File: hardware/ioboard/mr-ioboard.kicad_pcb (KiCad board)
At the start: 4 copper layers, 65 x 80 mm, 126 parts, among them J1 Conn_01x40_Shielded, J2 USB_C_Receptacle_USB2.0, J3 Conn_01x06, J4 Micro_SD_Card_Det, J5 Conn_01x04, J6 Conn_01x02, Q1 2N7002, SW1 SW_Push, U1 TPS62822, U10 F1C200S, U11 TPS54202DDC, U2 TPS56637, U3 TPD2E2U06, U4 DS90C363, U5 TPD2E2U06, U6 LD3985M28R_SOT23, U7 TPS62822, U8 FUSB302BMPX, U9 TPD2E2U06, Y1 24MHz

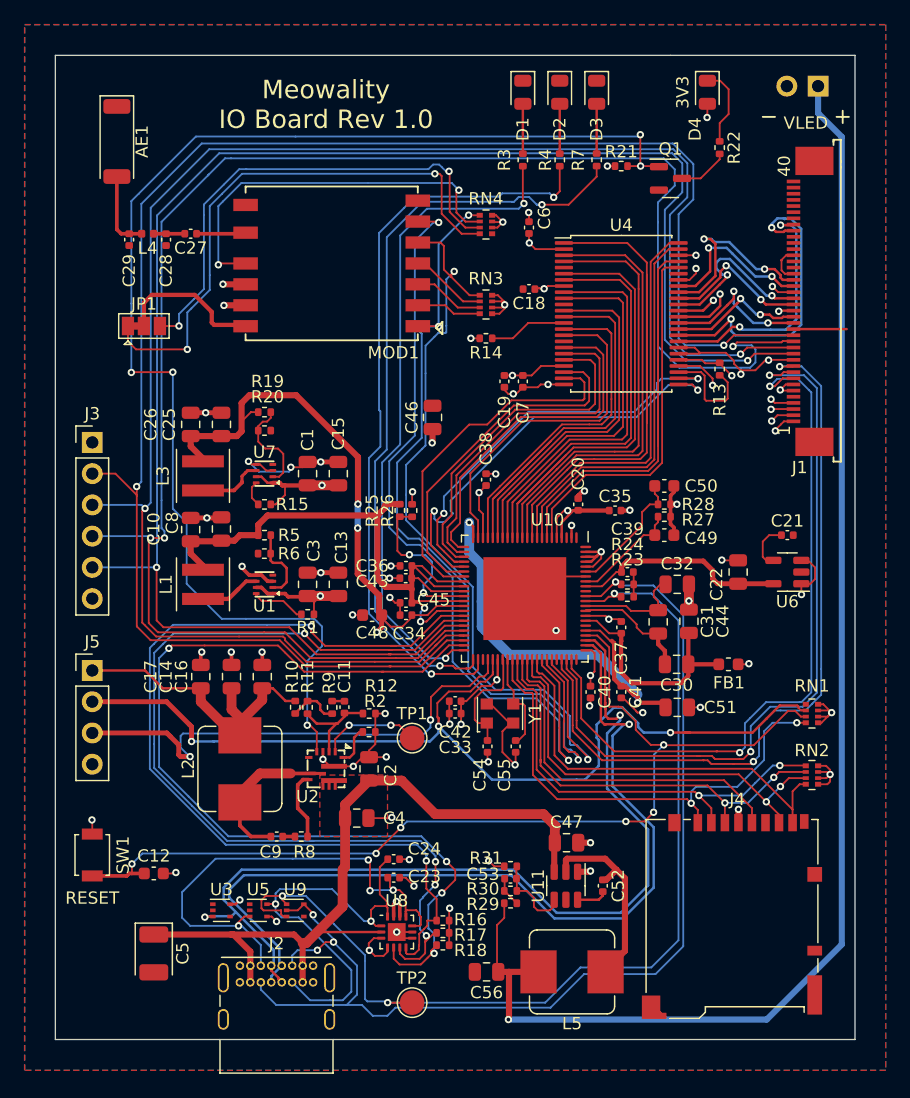
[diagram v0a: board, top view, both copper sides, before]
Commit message: Some tidying up of IO board
Signed-off-by: gatecat <gatecat@ds0.me>
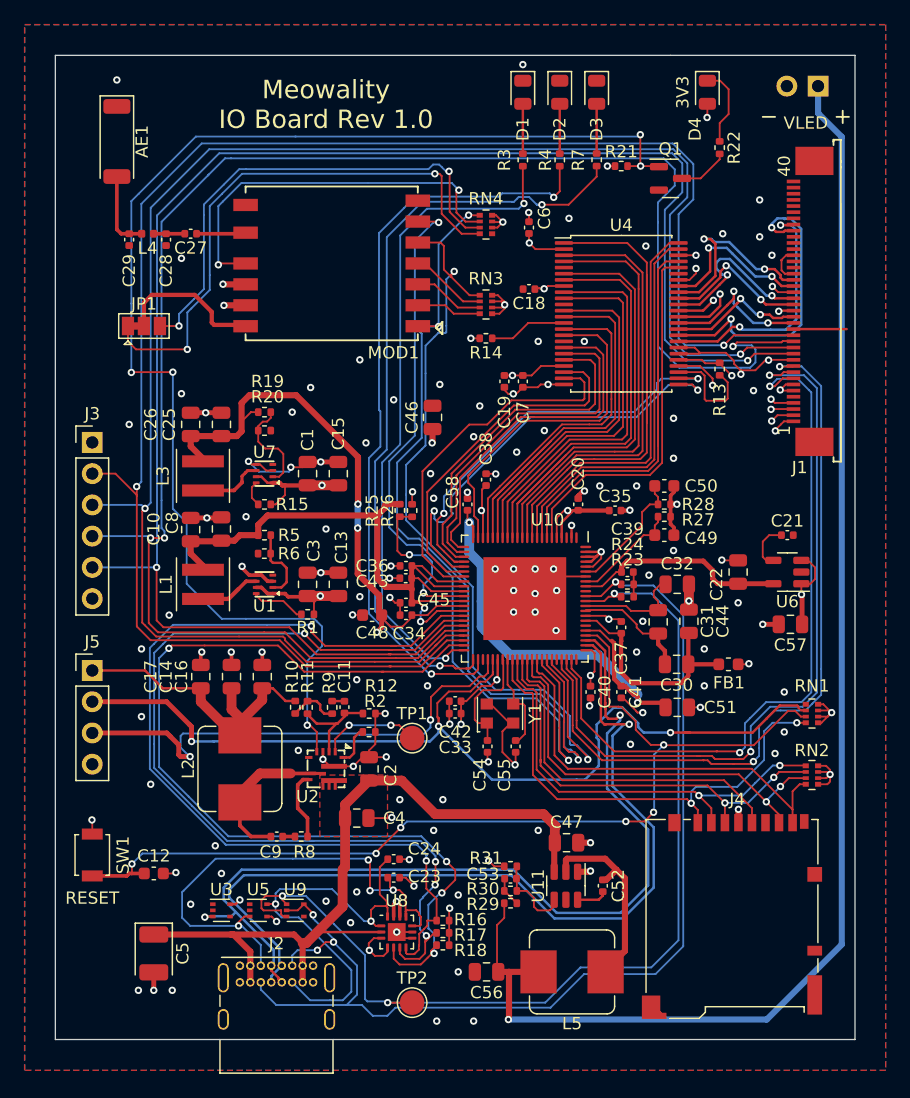
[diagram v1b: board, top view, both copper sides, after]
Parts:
- added C57: 10µ, Capacitor_SMD:C_0805_2012Metric, F.Cu at (159.8, 96.2)
- added C58: 470n, Capacitor_SMD:C_0402_1005Metric, F.Cu at (133.5, 86.5)
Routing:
- net GND: track 138.4 -> 141.6 mm, vias 57 -> 136
- net +3V3: track 138.3 -> 140.7 mm
- net +1V1: track 96.6 -> 97.7 mm

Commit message: Fix side of connector on IO board
Signed-off-by: gatecat <gatecat@ds0.me>
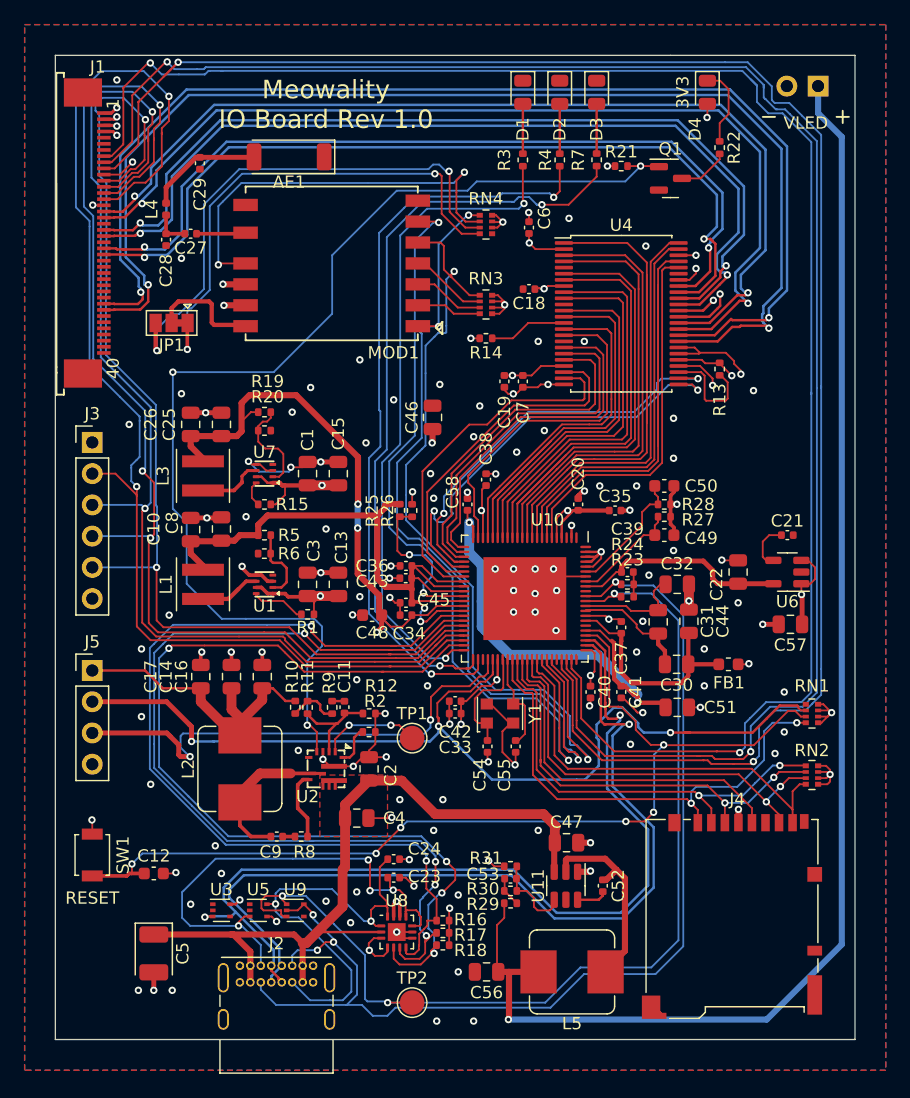
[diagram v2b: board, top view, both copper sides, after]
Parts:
- moved J1 56.3 mm to (103.9, 64.4), turned to -90 degrees
- moved AE1 14.1 mm to (119.0, 58.2), turned to 180 degrees
- moved C29 8.46 mm to (111.8, 58.8)
- moved L4 2.50 mm to (109.0, 62.5), turned to 90 degrees
- moved JP1 2.26 mm to (109.5, 71.8), turned to 180 degrees
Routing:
- net /FPGA_AUX0: track 61.6 -> 145.7 mm
- net /FPGA_AUX2: track 58.8 -> 141.0 mm
- net /FPGA_AUX1: track 61.2 -> 142.0 mm
- net /LVDS_CLK+: track 20.3 -> 97.1 mm
- net /LVDS_CLK-: track 25.0 -> 96.6 mm
- net /LVDS_D2+: track 11.1 -> 79.5 mm
- net /LVDS_D2-: track 12.4 -> 79.3 mm
- net /LVDS_D1-: track 12.8 -> 73.9 mm
- net /LVDS_D1+: track 14.4 -> 72.8 mm
- net /LVDS_D0-: track 13.3 -> 68.4 mm
- net /LVDS_D0+: track 16.0 -> 69.0 mm
- net /FPGA_JTAG_TDO: track 137.3 -> 89.3 mm
- net /FPGA_JTAG_TCK: track 143.0 -> 95.4 mm
- net /FPGA_JTAG_TDI: track 138.8 -> 92.9 mm
- net /FPGA_JTAG_TMS: track 140.1 -> 100.2 mm
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
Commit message: Fix IO board ERC/DRC issues
Signed-off-by: gatecat <gatecat@ds0.me>
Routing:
- net GND: track 127.7 -> 129.1 mm
- net /3V3_PG: vias 3 -> 2

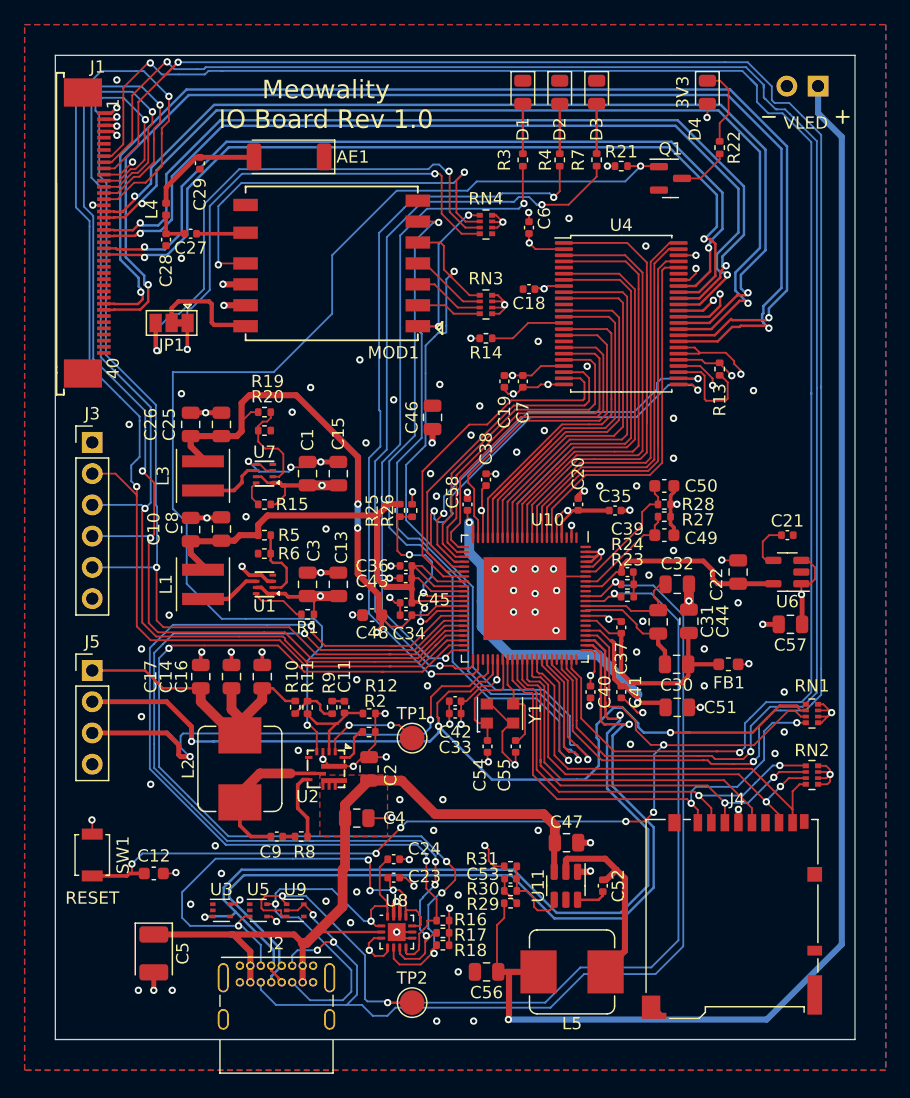
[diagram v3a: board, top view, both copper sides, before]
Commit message: Add mounting holes to IO board
Signed-off-by: gatecat <gatecat@ds0.me>
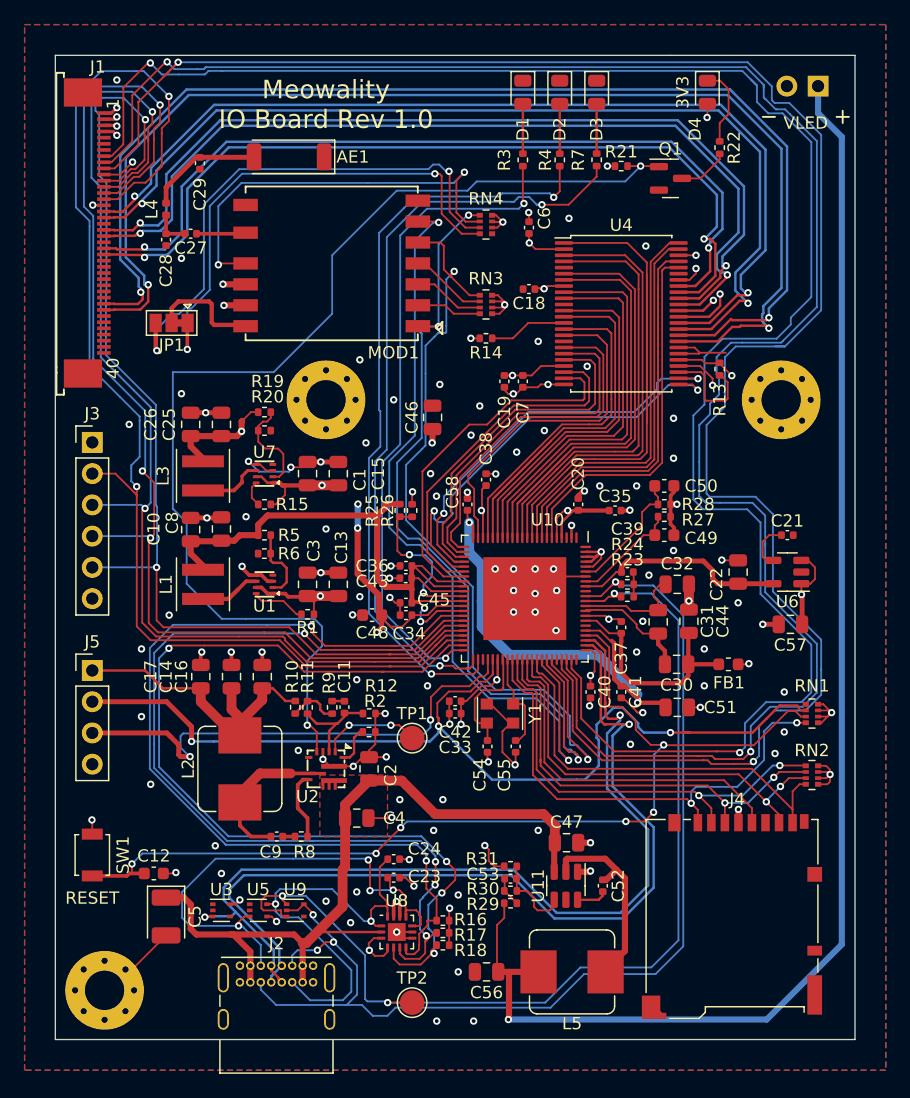
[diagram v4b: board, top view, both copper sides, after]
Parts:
- added H1: MountingHole_Pad, MountingHole:MountingHole_3.2mm_M3_Pad_Via, F.Cu at (122.0, 78.0)
- added H2: MountingHole_Pad, MountingHole:MountingHole_3.2mm_M3_Pad_Via, F.Cu at (159.0, 78.0)
- added H3: MountingHole_Pad, MountingHole:MountingHole_3.2mm_M3_Pad_Via, F.Cu at (104.0, 126.0)
- moved C5 3.16 mm to (109.0, 120.0)
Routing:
- net /FPGA_AUX0: track 145.7 -> 158.7 mm
- net /FPGA_AUX1: track 142.0 -> 154.9 mm
- net /FPGA_AUX2: track 141.0 -> 153.5 mm
- net +1V1: track 97.7 -> 92.7 mm, vias 5 -> 6
- net GND: track 129.1 -> 132.3 mm, vias 129 -> 121
- net /VBUS: track 63.1 -> 64.6 mm
